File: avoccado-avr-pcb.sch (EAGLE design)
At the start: 30 parts, among them IC1 MCP1703CB, IC5 ATMEGA328P-20MU, Q1 #MHz, Q2 MOSFET-NCHANNEL2N7002PW, U1 ATMEGA328P, U2 MCP73831, X1 Micro USB

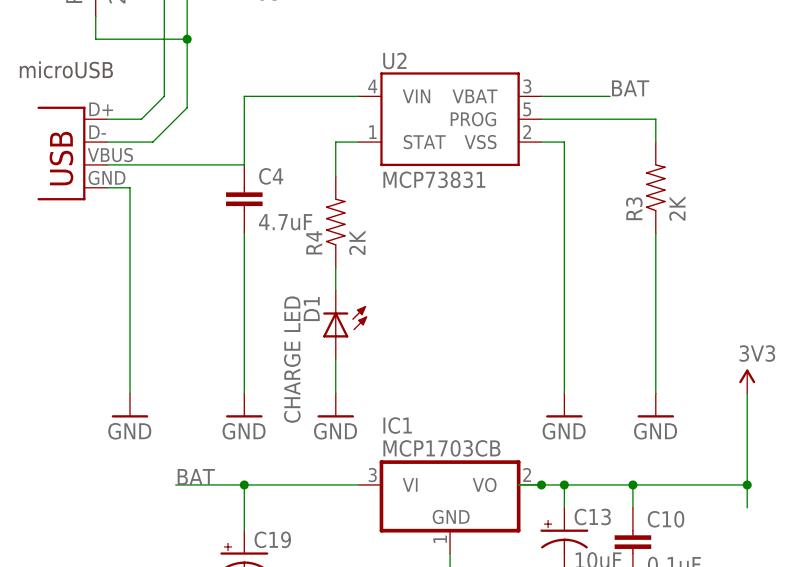
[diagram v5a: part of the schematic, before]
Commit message: charge indicator wired to MCU
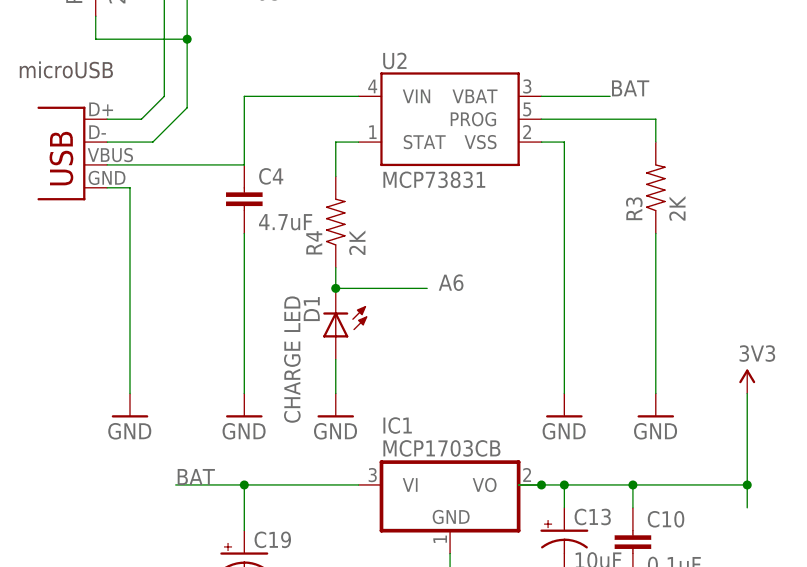
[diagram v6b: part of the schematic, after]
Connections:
- removed net N$5: D1.C, R4.1
- net A6: now also D1.C, R4.1
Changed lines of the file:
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@@
-</segment>
-</net>
-<net name="N$5" class="0">
-<segment>
-<pinref part="D1" gate="G$1" pin="C"/>
-<pinref part="R4" gate="G$1" pin="1"/>
-<wire x1="44.45" y1="134.62" x2="44.45" y2="137.16" width="0.1524" layer="91"/>
 </segment>
 </net>
@@
 <wire x1="152.4" y1="200.66" x2="167.64" y2="200.66" width="0.1524" layer="91"/>
 </segment>
+<segment>
+<wire x1="44.45" y1="134.874" x2="54.61" y2="134.874" width="0.1524" layer="91"/>
+<pinref part="D1" gate="G$1" pin="C"/>
+<pinref part="R4" gate="G$1" pin="1"/>
+<wire x1="44.45" y1="134.62" x2="44.45" y2="134.874" width="0.1524" layer="91"/>
+<wire x1="44.45" y1="134.874" x2="44.45" y2="137.16" width="0.1524" layer="91"/>
+<junction x="44.45" y="134.874"/>
+<label x="55.88" y="134.62" size="1.778" layer="95"/>
+</segment>
 </net>

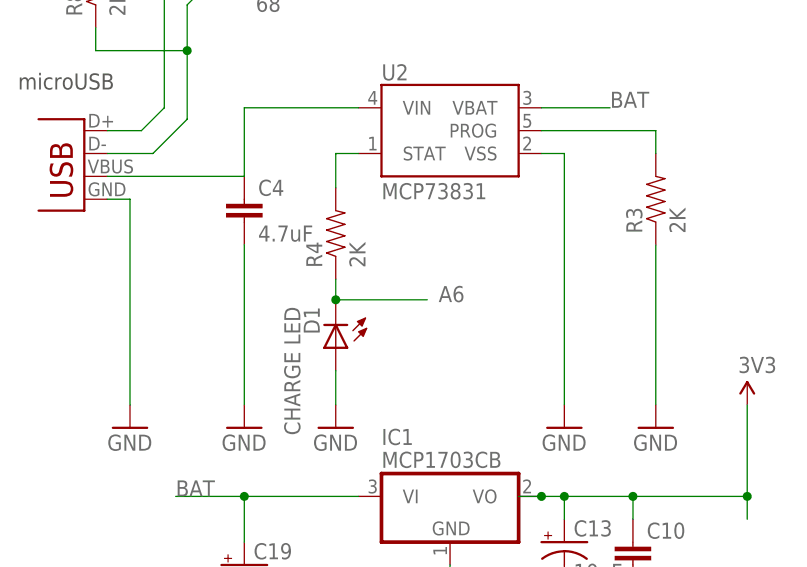
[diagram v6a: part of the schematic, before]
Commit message: reroute bottom header, reduce airwires
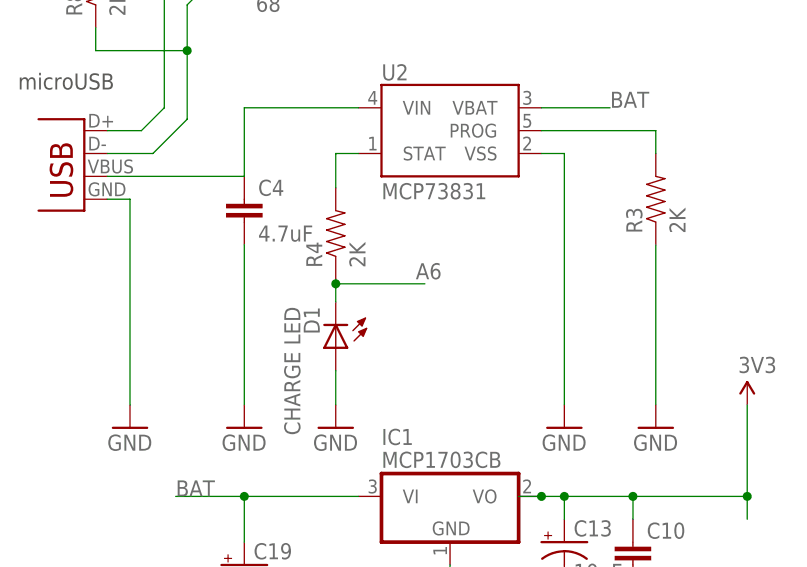
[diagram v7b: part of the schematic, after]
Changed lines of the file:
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@@
 </segment>
 <segment>
-<wire x1="44.45" y1="134.874" x2="54.61" y2="134.874" width="0.1524" layer="91"/>
 <pinref part="D1" gate="G$1" pin="C"/>
 <pinref part="R4" gate="G$1" pin="1"/>
-<wire x1="44.45" y1="134.62" x2="44.45" y2="134.874" width="0.1524" layer="91"/>
-<wire x1="44.45" y1="134.874" x2="44.45" y2="137.16" width="0.1524" layer="91"/>
-<junction x="44.45" y="134.874"/>
-<label x="55.88" y="134.62" size="1.778" layer="95"/>
+<wire x1="44.45" y1="134.62" x2="44.45" y2="136.652" width="0.1524" layer="91"/>
+<wire x1="44.45" y1="136.652" x2="44.45" y2="137.16" width="0.1524" layer="91"/>
+<wire x1="44.45" y1="136.652" x2="54.356" y2="136.652" width="0.1524" layer="91"/>
+<junction x="44.45" y="136.652"/>
+<label x="53.34" y="137.16" size="1.778" layer="95"/>
 </segment>
 </net>

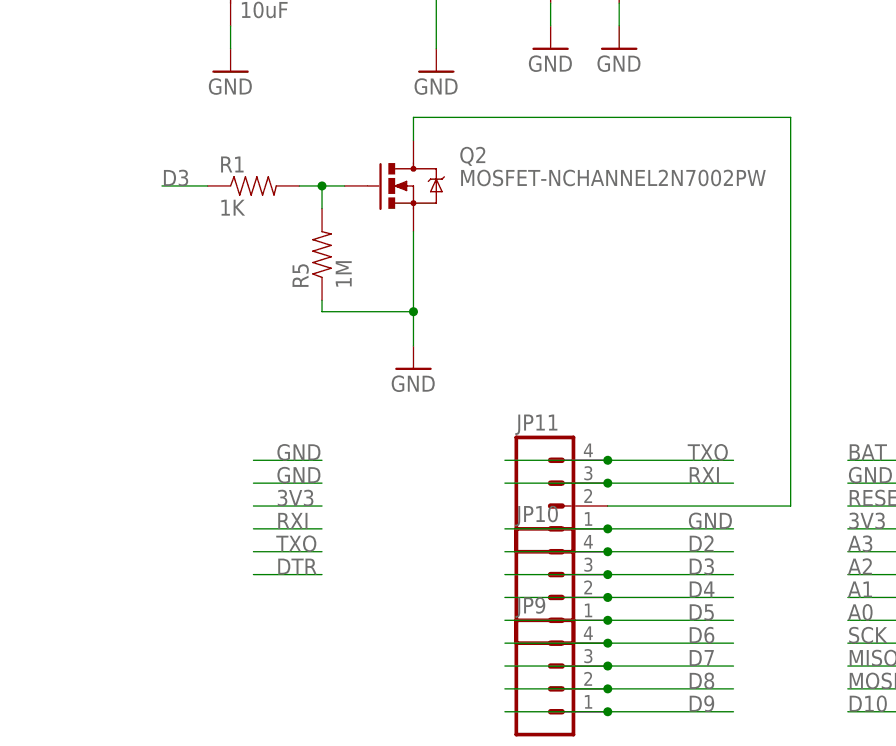
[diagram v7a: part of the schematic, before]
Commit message: reroute GND layer, ditch pins 2&3
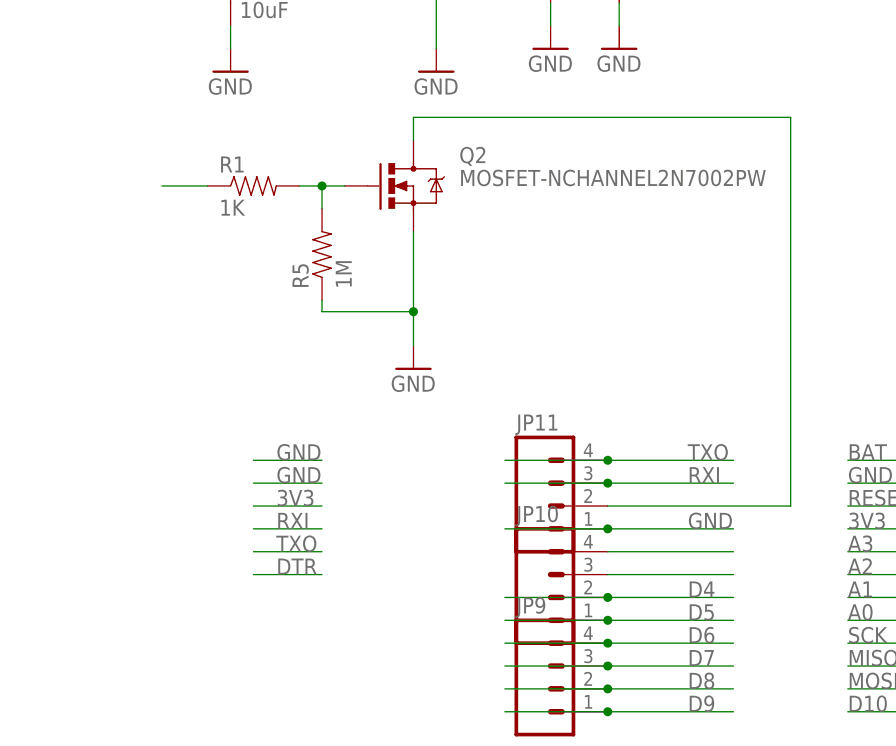
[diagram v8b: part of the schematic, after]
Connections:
- net D2: no longer JP10.4
- net D3: no longer JP10.3
- net GND: now also JP10.3, JP10.4
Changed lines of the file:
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@@
 <pinref part="GND16" gate="1" pin="GND"/>
+</segment>
+<segment>
+<wire x1="76.2" y1="41.91" x2="90.17" y2="41.91" width="0.1524" layer="91"/>
+<pinref part="JP10" gate="G$1" pin="4"/>
+</segment>
+<segment>
+<wire x1="76.2" y1="39.37" x2="90.17" y2="39.37" width="0.1524" layer="91"/>
+<pinref part="JP10" gate="G$1" pin="3"/>
 </segment>
 </net>
@@
 <net name="D2" class="0">
 <segment>
-<label x="85.09" y="41.91" size="1.778" layer="95"/>
-<wire x1="64.77" y1="41.91" x2="76.2" y2="41.91" width="0.1524" layer="91"/>
-<pinref part="JP10" gate="G$1" pin="4"/>
-<wire x1="76.2" y1="41.91" x2="90.17" y2="41.91" width="0.1524" layer="91"/>
-<junction x="76.2" y="41.91"/>
-</segment>
-<segment>
 <wire x1="215.9" y1="127" x2="226.06" y2="127" width="0.1524" layer="91"/>
 <label x="218.44" y="127" size="1.778" layer="95"/>
@@
 <net name="D3" class="0">
 <segment>
-<label x="85.09" y="39.37" size="1.778" layer="95"/>
-<wire x1="90.17" y1="39.37" x2="76.2" y2="39.37" width="0.1524" layer="91"/>
-<pinref part="JP10" gate="G$1" pin="3"/>
-<wire x1="76.2" y1="39.37" x2="64.77" y2="39.37" width="0.1524" layer="91"/>
-<junction x="76.2" y="39.37"/>
-<label x="26.67" y="82.55" size="1.778" layer="95"/>
-</segment>
-<segment>
 <wire x1="215.9" y1="124.46" x2="226.06" y2="124.46" width="0.1524" layer="91"/>
